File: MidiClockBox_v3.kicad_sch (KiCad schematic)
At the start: 57 parts, among them J1 WS2812, J10 Midi Out 5, J11 Midi Out 3, J12 Tap, J13 Start, J14 Stop, J15 Preset 1 Btn, J16 Preset 2 Btn, J17 Preset 3 Btn, J18 Preset 1 Sw, J19 Preset 2 Sw, J2 Display, J20 Preset 3 Sw, J21 Conn_02x01, J22 Conn_02x01, J23 Conn_02x01, J24 Conn_02x01, J25 Conn_02x01, J26 Conn_02x01, J27 Conn_02x01, J29 Midi IN, J3 Conn_02x12_Counter_Clockwise, J30 Midi Out 4, J4 Sync Out 0, J5 ICSP, J6 Midi Out 2, J7 Midi Out 1, J8 Midi Out 0, J9 Sync Out 1, SW1 RotaryEncoder_Switch, U1 74LS241, U2 CD74HC4067SM, U4 6N138

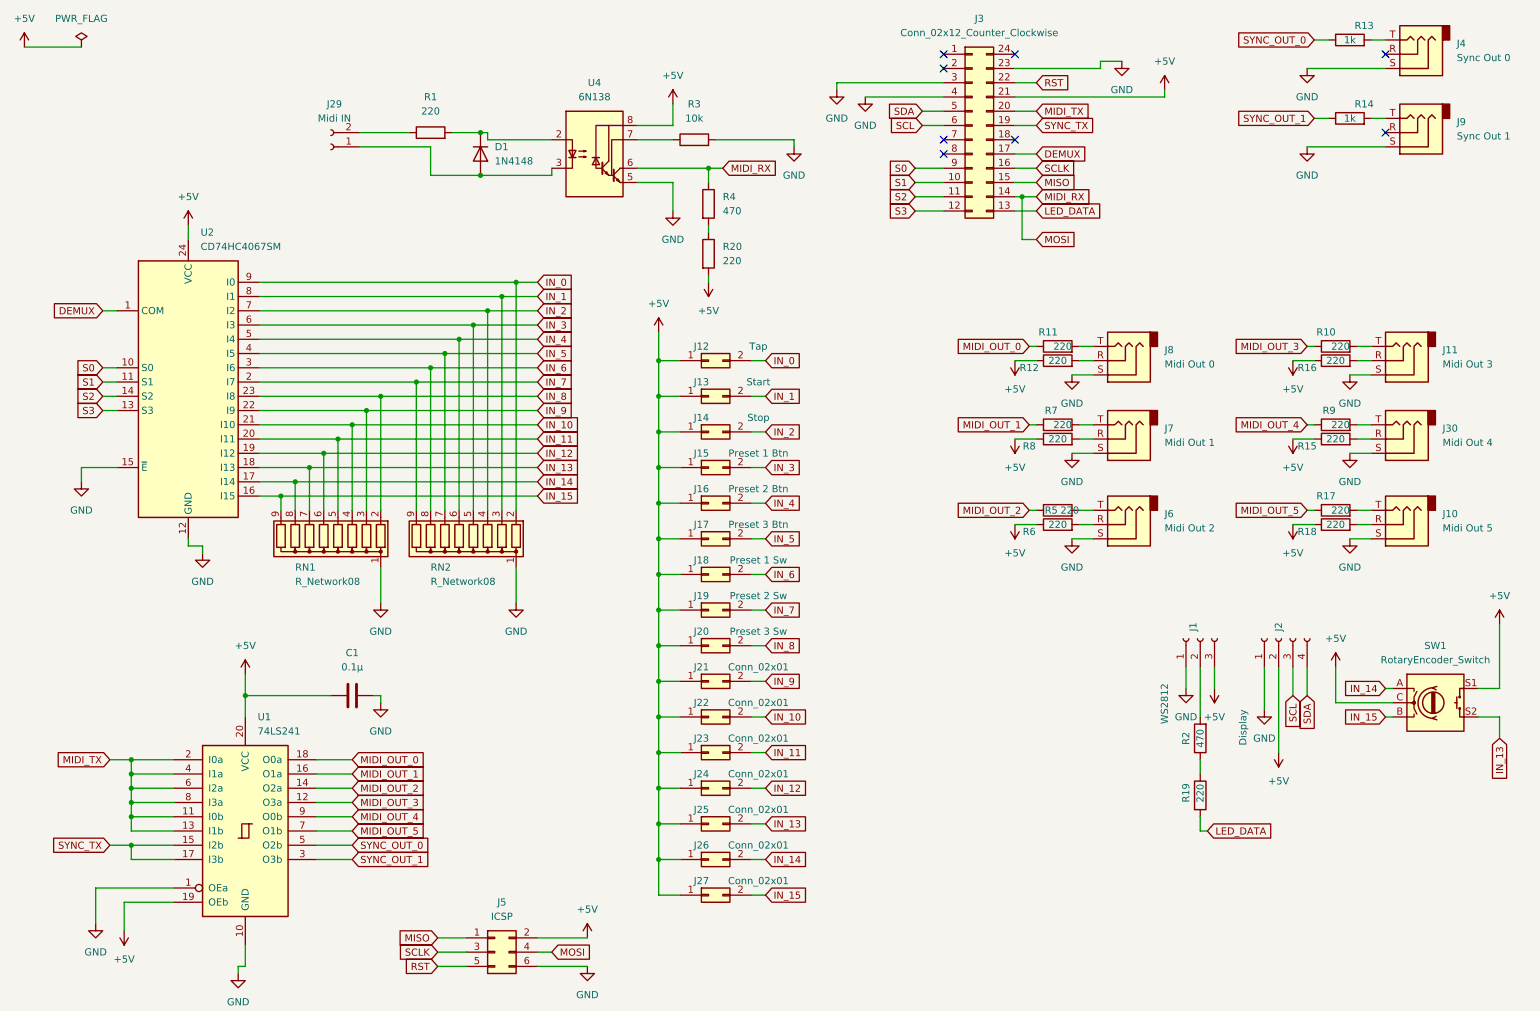
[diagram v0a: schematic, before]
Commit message: add circuit board design
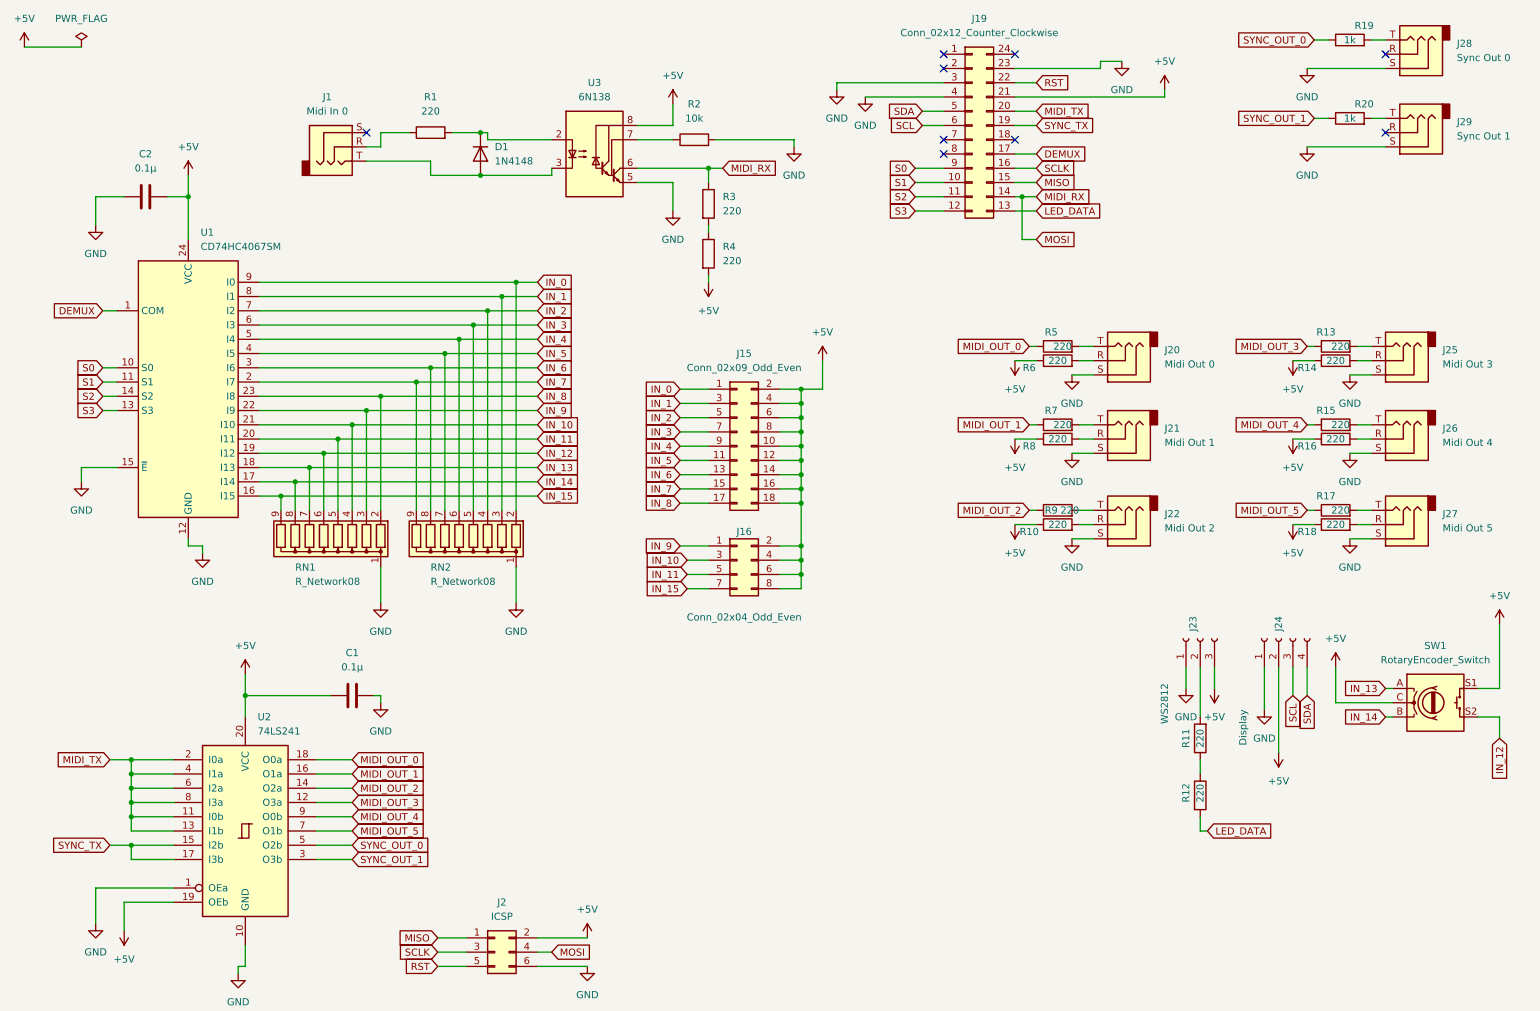
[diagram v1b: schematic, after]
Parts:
- removed J12: Tap, Connector_PinHeader_2.54mm:PinHeader_1x02_P2.54mm_Vertical, symbol Connector_Generic:Conn_02x01
- removed J13: Start, Connector_PinHeader_2.54mm:PinHeader_1x02_P2.54mm_Vertical, symbol Connector_Generic:Conn_02x01
- removed J14: Stop, Connector_PinHeader_2.54mm:PinHeader_1x02_P2.54mm_Vertical, symbol Connector_Generic:Conn_02x01
- removed J15: Preset 1 Btn, Connector_PinHeader_2.54mm:PinHeader_1x02_P2.54mm_Vertical, symbol Connector_Generic:Conn_02x01
- removed J16: Preset 2 Btn, Connector_PinHeader_2.54mm:PinHeader_1x02_P2.54mm_Vertical, symbol Connector_Generic:Conn_02x01
- removed J17: Preset 3 Btn, Connector_PinHeader_2.54mm:PinHeader_1x02_P2.54mm_Vertical, symbol Connector_Generic:Conn_02x01
- removed J18: Preset 1 Sw, Connector_PinHeader_2.54mm:PinHeader_1x02_P2.54mm_Vertical, symbol Connector_Generic:Conn_02x01
- removed J19: Preset 2 Sw, Connector_PinHeader_2.54mm:PinHeader_1x02_P2.54mm_Vertical, symbol Connector_Generic:Conn_02x01
- removed J20: Preset 3 Sw, Connector_PinHeader_2.54mm:PinHeader_1x02_P2.54mm_Vertical, symbol Connector_Generic:Conn_02x01
- removed J21, J22, J23, J24, J25, J26, J27: Conn_02x01, Connector_PinHeader_2.54mm:PinHeader_1x02_P2.54mm_Vertical, symbol Connector_Generic:Conn_02x01
- removed J29: Midi IN, Connector_PinHeader_2.54mm:PinHeader_1x02_P2.54mm_Vertical, symbol Connector:Conn_01x02_Socket
- added C2: 0.1µ, Capacitor_SMD:C_0201_0603Metric, symbol Device:C
- added J1: Midi In 0, Connector_Audio:Jack_3.5mm_CUI_SJ-3523-SMT_Horizontal, symbol Connector_Audio:AudioJack3
- added J15: Conn_02x09_Odd_Even, Connector_PinHeader_2.54mm:PinHeader_2x09_P2.54mm_Vertical, symbol Connector_Generic:Conn_02x09_Odd_Even
- added J16: Conn_02x04_Odd_Even, Connector_PinHeader_2.54mm:PinHeader_2x04_P2.54mm_Vertical, symbol Connector_Generic:Conn_02x04_Odd_Even
- R11: renamed from R2; value 470 -> 220
- R3: renamed from R4; value 470 -> 220
- renumbered J3 to J19, J5 to J2, J8 to J20, J7 to J21, J6 to J22, J1 to J23, J2 to J24, J11 to J25, J30 to J26, J10 to J27, J4 to J28, J9 to J29, R6 to R10, R19 to R12, R10 to R13, R16 to R14, R9 to R15, R15 to R16, R13 to R19, R3 to R2, R14 to R20, R20 to R4, R11 to R5, R12 to R6, R5 to R9, U2 to U1, U1 to U2, U4 to U3
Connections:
- net +5V: now also C2.1, J15.10 (Pin_10), J15.12 (Pin_12), J15.14 (Pin_14), J15.16 (Pin_16), J15.18 (Pin_18), J15.2 (Pin_2), J15.4 (Pin_4), J15.6 (Pin_6), J15.8 (Pin_8), J16.2 (Pin_2), J16.4 (Pin_4), J16.6 (Pin_6), J16.8 (Pin_8)
- net GND: now also C2.2
- net IN_0: now also J15.1 (Pin_1)
- net IN_1: now also J15.3 (Pin_3)
- net IN_10: now also J16.3 (Pin_3)
- net IN_11: now also J16.5 (Pin_5)
- net IN_12: now also SW1.S2
- net IN_13: now also SW1.A; no longer SW1.S2
- net IN_14: now also SW1.B; no longer SW1.A
- net IN_15: now also J16.7 (Pin_7); no longer SW1.B
- net IN_2: now also J15.5 (Pin_5)
- net IN_3: now also J15.7 (Pin_7)
- net IN_4: now also J15.9 (Pin_9)
- net IN_5: now also J15.11 (Pin_11)
- net IN_6: now also J15.13 (Pin_13)
- net IN_7: now also J15.15 (Pin_15)
- net IN_8: now also J15.17 (Pin_17)
- net IN_9: now also J16.1 (Pin_1)
- net at D1.2 (A), U3.3 (C2): now also J1.T
- net at R1.1: now also J1.R
- no-connect marks 8 -> 9

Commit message: switch resistor network for SMD parts
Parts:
- removed RN1, RN2: R_Network08, Resistor_THT:R_Array_SIP9, symbol Device:R_Network08
- added R1, R11, R12, R13, R14, R15, R16, R17, R2, R3, R4, R5, R6, R7, R8, R9: 10k, Resistor_SMD:R_0201_0603Metric, symbol Device:R
- renumbered C2 to C1, C1 to C2, J24 to J10, J25 to J11, J26 to J12, J27 to J13, J28 to J14, J29 to J15, J15 to J3, J16 to J4, J19 to J5, J20 to J6, J21 to J7, J22 to J8, J23 to J9, R1 to R10, R2 to R18, R3 to R19, R4 to R20, R5 to R21, R6 to R22, R7 to R23, R8 to R24, R9 to R25, R10 to R26, R11 to R27, R12 to R28, R13 to R29, R14 to R30, R15 to R31, R16 to R32, R17 to R33, R18 to R34, R19 to R35, R20 to R36
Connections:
- net GND: now also R1.2, R11.2, R12.2, R13.2, R14.2, R15.2, R16.2, R17.2, R2.2, R3.2, R4.2, R5.2, R6.2, R7.2, R8.2, R9.2
- net IN_0: now also R17.1
- net IN_1: now also R16.1
- net IN_10: now also R6.1
- net IN_11: now also R5.1
- net IN_12: now also R4.1
- net IN_13: now also R3.1
- net IN_14: now also R2.1
- net IN_15: now also R1.1
- net IN_2: now also R15.1
- net IN_3: now also R14.1
- net IN_4: now also R13.1
- net IN_5: now also R12.1
- net IN_6: now also R11.1
- net IN_7: now also R9.1
- net IN_8: now also R8.1
- net IN_9: now also R7.1

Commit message: switch SMD components form 0201-0603 to 0603-1608
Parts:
- C1, C2: footprint Capacitor_SMD:C_0201_0603Metric -> Capacitor_SMD:C_0603_1608Metric
- D1: footprint Diode_SMD:D_0201_0603Metric -> Diode_SMD:D_0603_1608Metric
- R1, R10, R11, R12, R13, R14, R15, R16, R17, R18, R19, R2, R20, R21, R22, R23, R24, R25, R26, R27, R28, R29, R3, R30, R31, R32, R33, R34, R35, R36, R4, R5, R6, R7, R8, R9: footprint Resistor_SMD:R_0201_0603Metric -> Resistor_SMD:R_0603_1608Metric

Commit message: add centroid archive
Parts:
- D1: footprint Diode_SMD:D_0603_1608Metric -> Diode_SMD:D_SOD-123
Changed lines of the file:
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@@
       (effects (font (size 1.27 1.27)) (justify left))
     )
-    (property "Footprint" "Diode_SMD:D_0603_1608Metric" (at 99.06 41.91 0)
+    (property "Footprint" "Diode_SMD:D_SOD-123" (at 99.06 41.91 0)
       (effects (font (size 1.27 1.27)) hide)
     )

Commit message: swtich to hardware serial
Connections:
- net MIDI_RX: now also J5.2 (Pin_2); no longer J2.4 (Pin_4), J5.14 (Pin_14)
- net MIDI_TX: now also J5.1 (Pin_1); no longer J5.20 (Pin_20)
- new net MOSI: J2.4 (Pin_4), J5.14 (Pin_14)
- no-connect marks 9 -> 8
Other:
- note added: "Independent midi out sync out extra pin for START STOP"

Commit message: add comments for stuff 2do
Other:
- note added: "Hardware midi in/ out Independent midi out -> demultiplex sync out extra pin for START STOP board targeted for case-use"
- note removed: "Independent midi out sync out extra pin for START STOP"
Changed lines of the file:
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@@
 		)
 	)
-	(text "Independent midi out\n\nsync out extra pin for START STOP"
+	(text "Hardware midi in/ out\nIndependent midi out -> demultiplex\nsync out extra pin for START STOP\nboard targeted for case-use\n"
 		(exclude_from_sim no)
 		(at 227.33 172.974 0)

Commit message: add stuff
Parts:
- added C3, C4, C5, C6, C7: 0.1µ, Capacitor_SMD:C_0603_1608Metric, symbol Device:C
- added J16: Conn_01x08, Connector_PinHeader_2.54mm:PinHeader_1x08_P2.54mm_Vertical, symbol Connector_Generic:Conn_01x08
- added U4: 74HC595, Package_SO:TSSOP-28_6.1x9.7mm_P0.65mm, symbol 74xx:74HC595
- added U6, U7: 74LS08, symbol 74xx:74LS08
- added U8: 74HC595, symbol 74xx:74HC595
- added U9: 74LS241, Package_SO:SOIC-20W_7.5x12.8mm_P1.27mm, symbol 74xx:74LS241
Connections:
- net +5V: now also C3.1, C4.1, C5.1, C6.1, C7.1, J16.7 (Pin_7), U4.10 (~{SRCLR}), U4.16 (VCC), U6.14 (VCC), U7.14 (VCC), U8.10 (~{SRCLR}), U8.16 (VCC), U9.19 (OEb), U9.20 (VCC)
- net GND: now also C3.2, C4.2, C5.2, C6.2, C7.2, J16.8 (Pin_8), U4.13 (~{OE}), U4.8 (GND), U6.7 (GND), U7.7 (GND), U8.13 (~{OE}), U8.8 (GND), U9.1 (OEa), U9.10 (GND)
- net MIDI_TX: now also U6.1, U6.12, U6.4, U6.9, U7.1, U7.9; no longer U2.11 (I0b), U2.13 (I1b), U2.2 (I0a), U2.4 (I1a), U2.6 (I2a), U2.8 (I3a)
- net SYNC_TX: now also U7.12, U7.4; no longer U2.15 (I2b), U2.17 (I3b)
- net SYNC_START_STOP_BUFFERED_1: now reaches J15.R
- net SYNC_START_STOP_BUFFERED_1: now also U9.16 (O1a)
- net DA2: now reaches J5.18 (Pin_18)
- net DA2: now also U4.12 (RCLK), U8.12 (RCLK)
- net SYNC_START_STOP: now reaches J5.20 (Pin_20)
- net SYNC_START_STOP: now also U9.2 (I0a), U9.4 (I1a)
- net DA0: now reaches J5.7 (Pin_7)
- net DA0: now also U8.14 (SER)
- net DA1: now reaches J5.8 (Pin_8)
- net DA1: now also U4.11 (SRCLK), U8.11 (SRCLK)
- net SYNC_START_STOP_BUFFERED_0: now reaches J14.R
- net SYNC_START_STOP_BUFFERED_0: now also U9.18 (O0a)
- net SYNC_OUT_0 renamed SYNC_TX_BUFFERED_0
- net SYNC_OUT_1 renamed SYNC_TX_BUFFERED_1
- new net: U2.11 (I0b), U7.3
- new net: U2.13 (I1b), U7.8
- new net: U2.15 (I2b), U7.11
- new net: U2.17 (I3b), U7.6
- new net: U2.2 (I0a), U6.3
- new net: U2.4 (I1a), U6.6
- new net: U2.6 (I2a), U6.8
- new net: U2.8 (I3a), U6.11
- new net: J16.1 (Pin_1), U9.14 (O2a)
- new net: J16.2 (Pin_2), U9.12 (O3a)
- new net: J16.3 (Pin_3), U9.9 (O0b)
- new net: J16.4 (Pin_4), U9.7 (O1b)
- new net: J16.5 (Pin_5), U9.5 (O2b)
- new net: J16.6 (Pin_6), U9.3 (O3b)
- new net: U6.2, U8.15 (QA)
- new net: U7.13, U8.6 (QG)
- new net: U4.1 (QB), U9.8 (I3a)
- new net: U4.14 (SER), U8.9 (QH')
- new net: U4.15 (QA), U9.6 (I2a)
- new net: U4.2 (QC), U9.11 (I0b)
- new net: U4.3 (QD), U9.13 (I1b)
- new net: U4.4 (QE), U9.15 (I2b)
- new net: U4.5 (QF), U9.17 (I3b)
- new net: U6.13, U8.3 (QD)
- new net: U7.5, U8.7 (QH)
- new net: U6.10, U8.2 (QC)
- new net: U6.5, U8.1 (QB)
- new net: U7.10, U8.5 (QF)
- new net: U7.2, U8.4 (QE)
- no-connect marks 8 -> 5
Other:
- note added: "D19 / A1"
- note added: "D4 / A6"
- note added: "D5"
- note added: "Hardware midi in/ out: check Independent midi out -> demultiplex: check sync out extra pin for START STOP: check board targeted for case-use Potentialfreie Kontakte"
- note added: "Pre-load MIDI and SYNC outputs"
- note added: "SYNC START STOP sind nicht unabhängig, aber es gibt 6 gepufferte Ausgänge mit VCC und GND zum Forschen"
- note removed: "Hardware midi in/ out Independent midi out -> demultiplex sync out extra pin for START STOP board targeted for case-use"
- moved on the sheet: C1, C2, D1, J1, J10, J11, J12, J13, J14, J15, J2, J3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

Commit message: add parts to pcb
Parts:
- U4: footprint Package_SO:TSSOP-28_6.1x9.7mm_P0.65mm -> Package_SO:SO-16_3.9x9.9mm_P1.27mm
- U6, U7: footprint (none) -> Package_SO:SO-14_3.9x8.65mm_P1.27mm
- U8: footprint (none) -> Package_SO:SO-16_3.9x9.9mm_P1.27mm
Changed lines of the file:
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@@
 			)
 		)
-		(property "Footprint" ""
+		(property "Footprint" "Package_SO:SO-14_3.9x8.65mm_P1.27mm"
 			(at 39.37 181.61 0)
 			(effects
@@
 			)
 		)
-		(property "Footprint" ""
+		(property "Footprint" "Package_SO:SO-14_3.9x8.65mm_P1.27mm"
 			(at 39.37 234.95 0)
 			(effects
@@
 			)
 		)
-		(property "Footprint" ""
+		(property "Footprint" "Package_SO:SO-14_3.9x8.65mm_P1.27mm"
 			(at 99.06 114.3 0)
 			(effects
@@
 			)
 		)
-		(property "Footprint" ""
+		(property "Footprint" "Package_SO:SO-14_3.9x8.65mm_P1.27mm"
 			(at 99.06 167.64 0)
 			(effects
@@
 			)
 		)
-		(property "Footprint" "Package_SO:TSSOP-28_6.1x9.7mm_P0.65mm"
+		(property "Footprint" "Package_SO:SO-16_3.9x9.9mm_P1.27mm"
 			(at 74.93 210.82 0)
 			(effects
@@
 			)
 		)
-		(property "Footprint" ""
+		(property "Footprint" "Package_SO:SO-14_3.9x8.65mm_P1.27mm"
 			(at 99.06 140.97 0)
 			(effects
@@
 			)
 		)
-		(property "Footprint" ""
+		(property "Footprint" "Package_SO:SO-14_3.9x8.65mm_P1.27mm"
 			(at 99.06 176.53 0)
 			(effects
@@
 			)
 		)
-		(property "Footprint" ""
+		(property "Footprint" "Package_SO:SO-14_3.9x8.65mm_P1.27mm"
 			(at 99.06 132.08 0)
 			(effects
@@
 			)
 		)
-		(property "Footprint" ""
+		(property "Footprint" "Package_SO:SO-14_3.9x8.65mm_P1.27mm"
 			(at 99.06 123.19 0)
 			(effects
@@
 			)
 		)
-		(property "Footprint" ""
+		(property "Footprint" "Package_SO:SO-14_3.9x8.65mm_P1.27mm"
 			(at 99.06 158.75 0)
 			(effects
@@
 			)
 		)
-		(property "Footprint" ""
+		(property "Footprint" "Package_SO:SO-16_3.9x9.9mm_P1.27mm"
 			(at 64.77 133.35 0)
 			(effects
@@
 			)
 		)
-		(property "Footprint" ""
+		(property "Footprint" "Package_SO:SO-14_3.9x8.65mm_P1.27mm"
 			(at 99.06 149.86 0)
 			(effects
